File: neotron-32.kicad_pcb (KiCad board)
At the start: 2 copper layers, 166.9 x 140.7 mm, 95 parts, among them J1 Conn_02x06, J10 micro SD Card, J11 Conn_02x13_Top_Bottom, J12 AVR-ISP-6, J13 DE9 Male, J14 DE9 Male, J15 Double-mini-DIN-6, J17 DB15HD_Female, J18 Conn_02x05, J2 Conn_02x06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

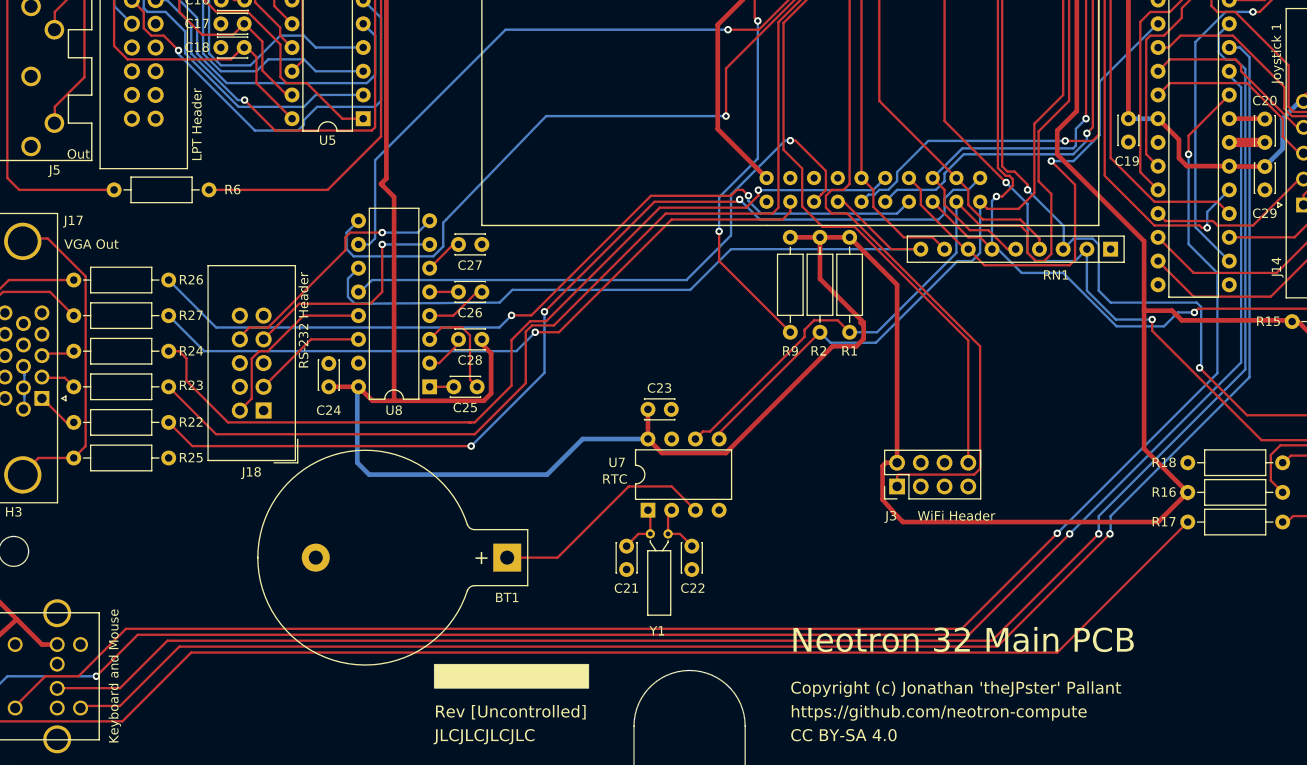
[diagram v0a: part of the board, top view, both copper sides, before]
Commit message: Moved some tracks away from the Neotron silkscreen text.
Also removed some weird trace overlaps near the Wifi connector.
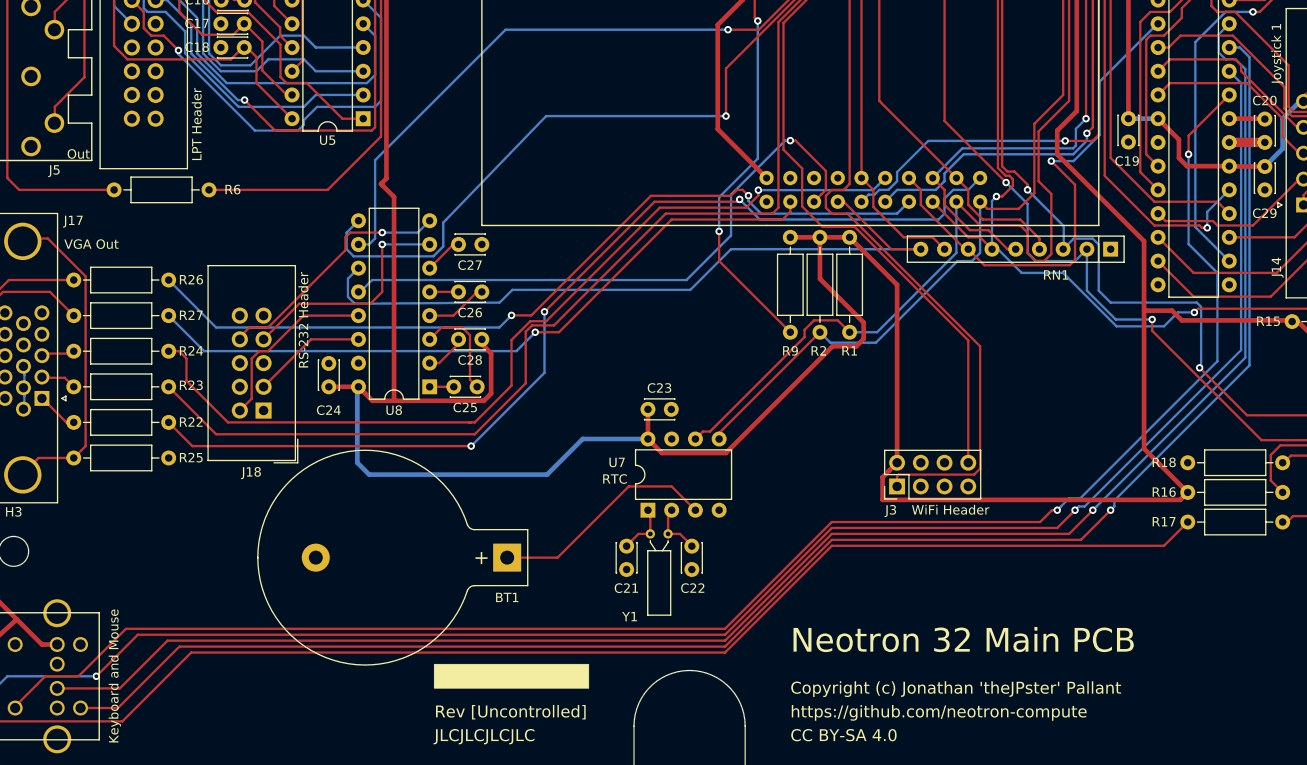
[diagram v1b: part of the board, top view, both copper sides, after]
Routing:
- net +3V3: track 498.1 -> 494.0 mm
- net /Keyboard, Mouse and Joystick/MS_DAT: track 181.7 -> 179.9 mm
- net /Keyboard, Mouse and Joystick/MS_CLK: track 177.7 -> 176.3 mm
- net /Keyboard, Mouse and Joystick/KB_DAT: track 179.9 -> 179.1 mm
- net /Keyboard, Mouse and Joystick/KB_CLK: track 176.4 -> 175.7 mm

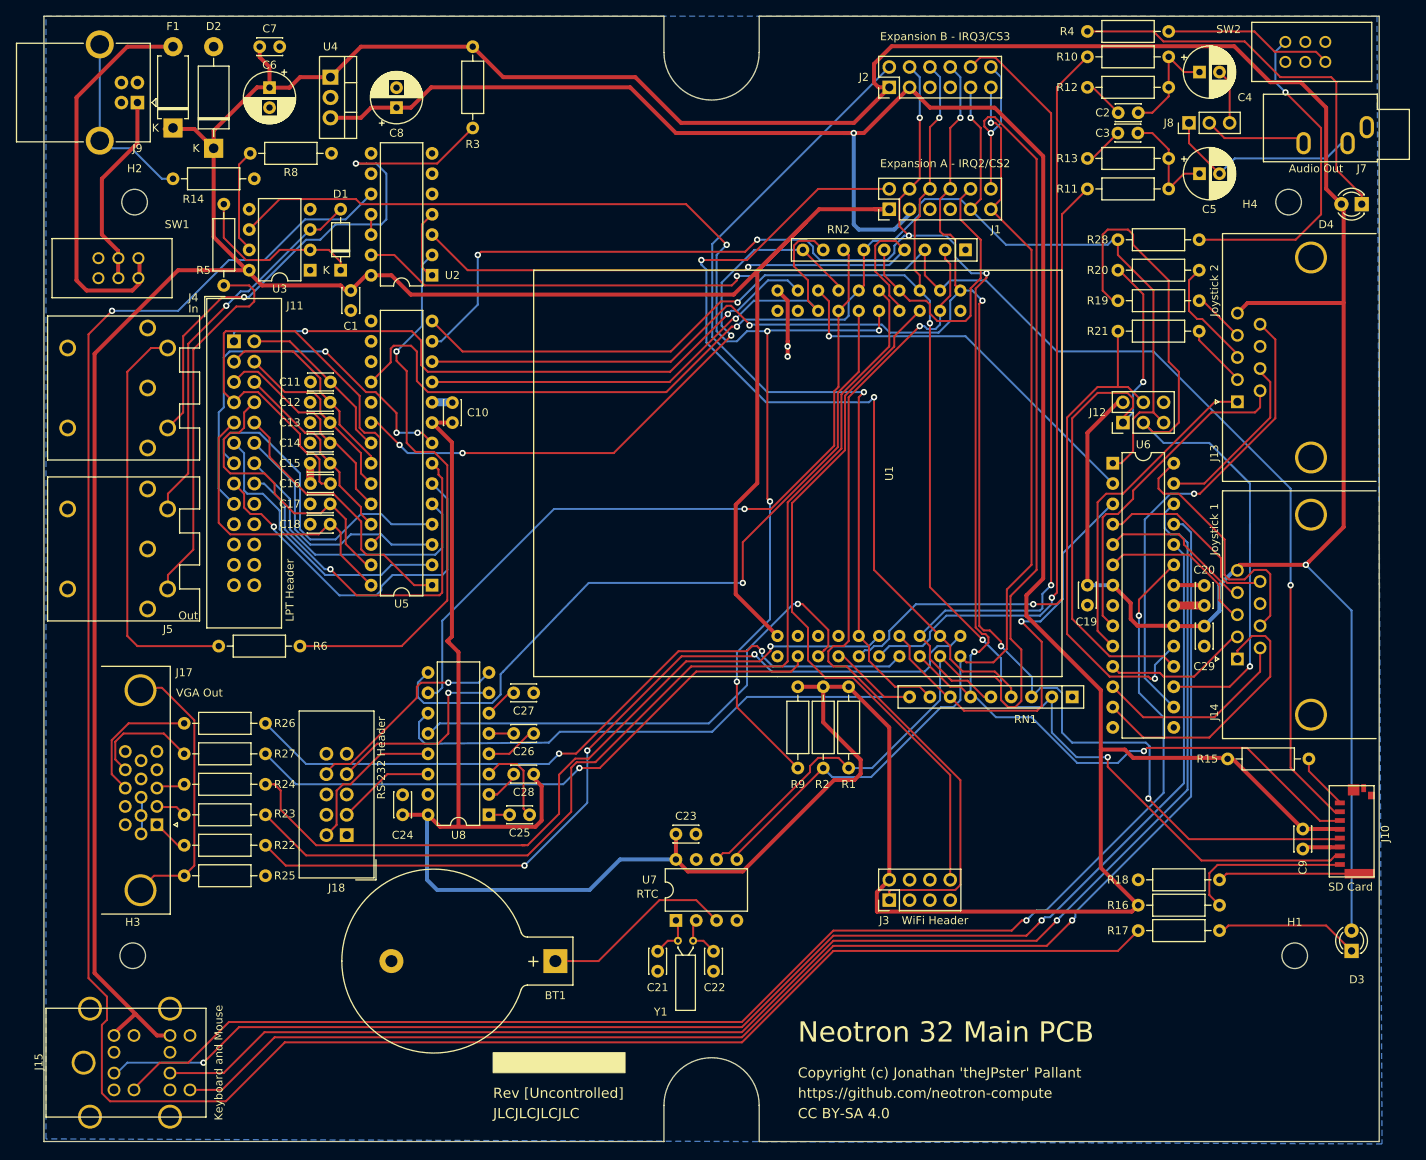
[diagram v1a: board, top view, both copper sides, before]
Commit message: Laying out board again, but on a 50 mil grid for parts.
Will use 25 mil grid for traces. This will hopefully avoid the issue
of traces 'sticking' to legs rather than cleanly going precisely down
the middle. It also looks a lot nicer now everything is properly
aligned.

I've also taken the opportunity to put the expansion slots all next to each other.
Might need to add some support holes for some legs, a la M.2 SSDs.
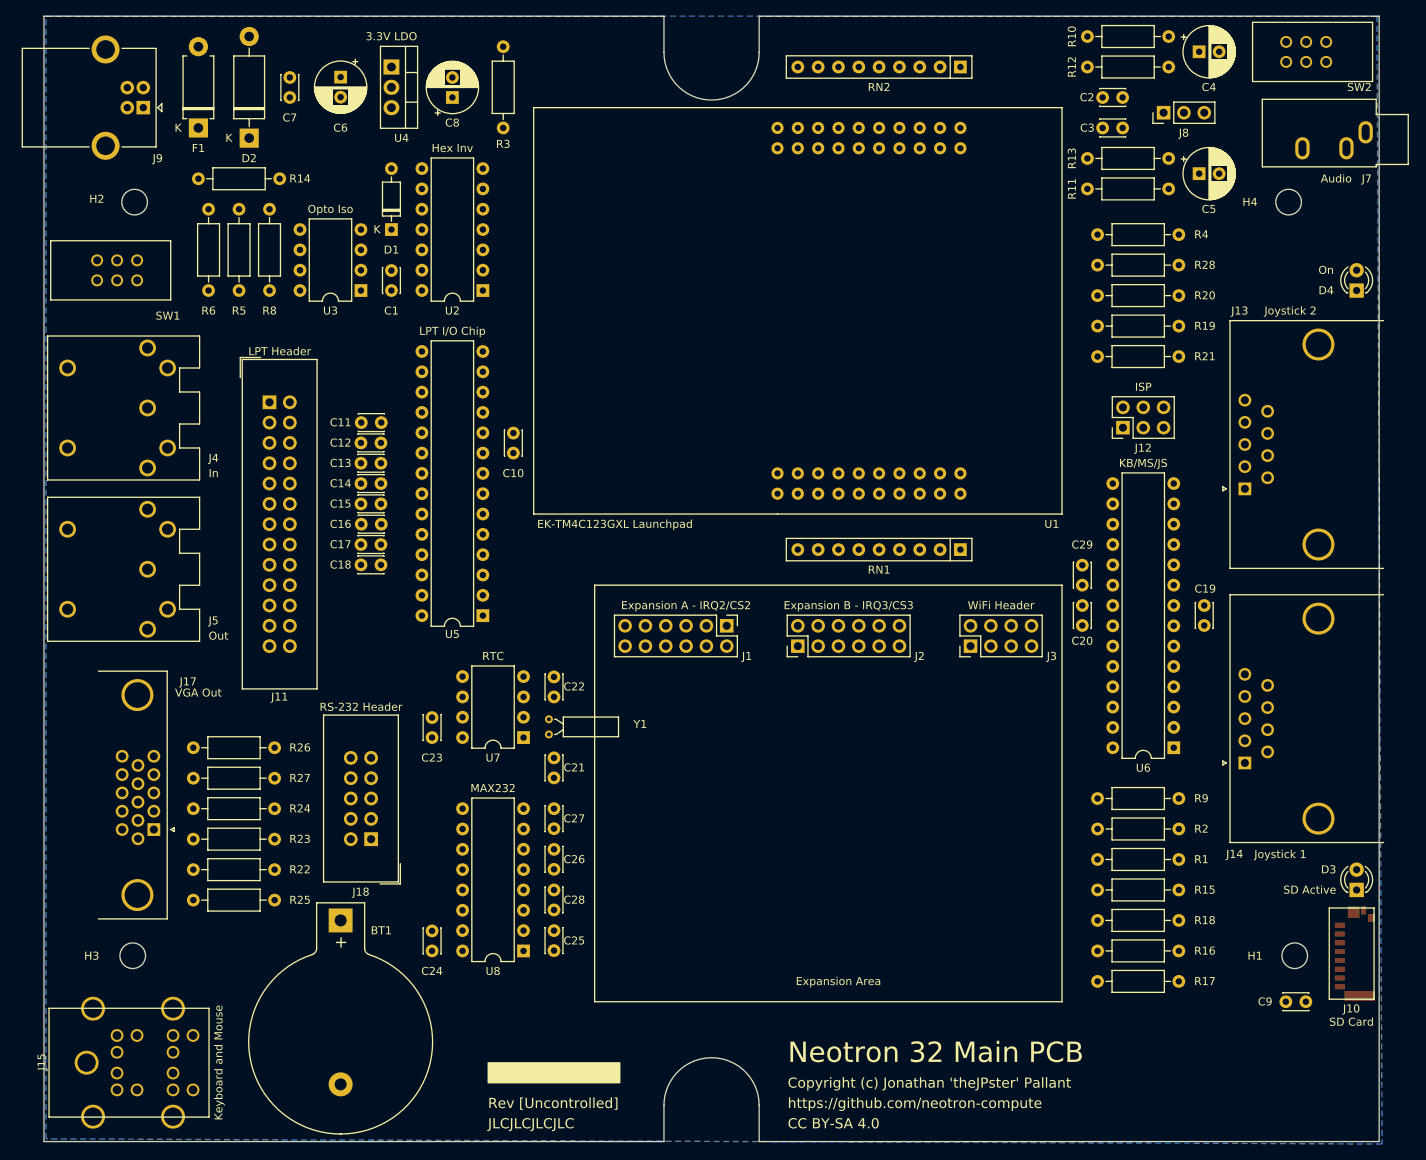
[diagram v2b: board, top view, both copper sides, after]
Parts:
- moved J2 70.8 mm to (165.1, 96.5)
- moved J1 55.9 mm to (156.2, 94.0), turned to 270 degrees
- moved R6 55.8 mm to (91.4, 41.9), turned to 270 degrees
- moved R9 37.7 mm to (202.6, 115.6), turned to 0 degrees
- moved C22 37.5 mm to (134.6, 102.9), turned to 90 degrees
- moved U6 36.4 mm to (212.1, 109.2), turned to 180 degrees
- moved R2 35.1 mm to (202.6, 119.4), turned to 0 degrees
- moved J3 33.3 mm to (186.7, 96.5)
- moved R1 33.1 mm to (202.6, 123.2), turned to 0 degrees
- moved C23 32.8 mm to (119.4, 108.0), turned to 90 degrees
- moved Y1 30.4 mm to (134.0, 107.6), turned to 90 degrees
- moved U7 29.8 mm to (130.8, 108.0), turned to 180 degrees
- moved C21 27.4 mm to (134.6, 113.0)
- moved BT1 27.3 mm to (108.0, 130.8), turned to 270 degrees
- moved R4 25.4 mm to (202.6, 45.1)
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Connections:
- net Net-(F1-Pad2) renamed /Power/UNFUSED_5V
- net Net-(J9-Pad1) renamed /Power/VUSB
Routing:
- net +5V: track 638.8 -> 0.00 mm, vias 1 -> 0
- net +3V3: track 494.0 -> 0.00 mm, vias 1 -> 0
- net Net-(R17-Pad2): track 277.5 -> 0.00 mm, vias 1 -> 0
- net /PA5_SPI_MOSI: track 226.1 -> 0.00 mm, vias 7 -> 0
- net /PA2_SPI_CLK: track 215.4 -> 0.00 mm, vias 5 -> 0
- net /PA4_SPI_MISO: track 208.3 -> 0.00 mm, vias 5 -> 0
- net /Keyboard, Mouse and Joystick/MS_DAT: track 179.9 -> 0.00 mm, vias 1 -> 0
- net /Keyboard, Mouse and Joystick/KB_DAT: track 179.1 -> 0.00 mm, vias 2 -> 0
- net /~PA3_SPI_CS0: track 177.7 -> 0.00 mm, vias 2 -> 0
- net /Keyboard, Mouse and Joystick/MS_CLK: track 176.3 -> 0.00 mm, vias 1 -> 0
- net /Keyboard, Mouse and Joystick/KB_CLK: track 175.7 -> 0.00 mm, vias 2 -> 0
- net /~RESET: track 169.7 -> 0.00 mm, vias 2 -> 0
- net /PC6_MIDI_IN: track 158.4 -> 0.00 mm, vias 5 -> 0
- net /PA6_I2C_SCL: track 154.3 -> 0.00 mm, vias 1 -> 0
- net /PB7_VGA_GREEN: track 132.8 -> 0.00 mm
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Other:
- net class Default: clearance 0.2 -> 0.254; trace_width 0.25 -> 0.254; via_dia 0.8 -> 1.016; via_drill 0.4 -> 0.635
- net class Power: clearance 0.2 -> 0.381; trace_width 0.5 -> 0.508; via_dia 0.8 -> 1.016; via_drill 0.4 -> 0.635
- rule pad_to_mask_clearance: 0.051 -> 0.0508
- rule solder_mask_min_width: 0.25 -> 0.254
- rule trace_clearance: 0.2 -> 0.254
- rule trace_min: 0.2 -> 0.2032
- rule via_min_drill: 0.3 -> 0.3048
- rule via_min_size: 0.4 -> 0.4064
- board text added: "3.3V LDO"
- board text added: "Audio"
- board text added: "EK-TM4C123GXL Launchpad"
- board text added: "Expansion Area"
- board text added: "Hex Inv"
- board text added: "ISP"
- board text added: "KB/MS/JS"
- board text added: "LPT I/O Chip"
- board text added: "MAX232"
- board text added: "On"
- board text added: "Opto Iso"
- board text added: "SD Active"
- board text removed: "Audio Out"

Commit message: Work in progress.
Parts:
- added H5: MountingHole, MountingHole:MountingHole_3.2mm_M3, F.Cu at (149.9, 134.6)
- added H6: MountingHole, MountingHole:MountingHole_3.2mm_M3, F.Cu at (171.4, 134.6)
- moved R9 80.3 mm to (175.3, 40.0), turned to 180 degrees
- moved R3 41.7 mm to (95.2, 57.1), turned to 0 degrees
- moved J2 13.0 mm to (177.8, 94.0), turned to 270 degrees
- moved D4 2.54 mm to (234.9, 49.5), turned to 270 degrees
- moved J7 0.85 mm to (235.2, 32.3)
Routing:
- net +5V: track 0.00 -> 493.0 mm
- net +3V3: track 0.00 -> 191.4 mm
- net /~RESET: track 0.00 -> 177.6 mm
- net /PA7_I2C_SDA: track 0.00 -> 112.0 mm, vias 0 -> 1
- net /PA6_I2C_SCL: track 0.00 -> 111.8 mm
- net /~PA3_SPI_CS0: track 0.00 -> 101.0 mm, vias 0 -> 1
- net Net-(R28-Pad2): track 0.00 -> 83.5 mm
- net /PA4_SPI_MISO: track 0.00 -> 73.2 mm, vias 0 -> 2
- net /PA2_SPI_CLK: track 0.00 -> 70.8 mm, vias 0 -> 2
- net /PE5_AUDIO_R: track 0.00 -> 69.0 mm
- net /Keyboard, Mouse and Joystick/SELECT_JS2: track 0.00 -> 68.8 mm
- net /PA5_SPI_MOSI: track 0.00 -> 67.8 mm, vias 0 -> 1
- net Net-(J9-Pad5): track 0.00 -> 57.1 mm
- net /PE4_AUDIO_L: track 0.00 -> 55.7 mm
- net /~PE3_IRQ2: track 0.00 -> 53.2 mm
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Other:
- net class Power: clearance 0.381 -> 0.254
- rule pad_to_mask_clearance: 0.0508 -> 0.0254

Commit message: Work tracing done.
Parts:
- moved R17 7.62 mm to (212.7, 130.8)
- moved R18 7.62 mm to (212.7, 138.4)
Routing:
- net /Keyboard, Mouse and Joystick/KB_CLK: track 0.00 -> 178.3 mm, vias 0 -> 1
- net /Keyboard, Mouse and Joystick/KB_DAT: track 0.00 -> 168.8 mm, vias 0 -> 1
- net /Keyboard, Mouse and Joystick/MS_DAT: track 0.00 -> 166.4 mm, vias 0 -> 1
- net /Keyboard, Mouse and Joystick/MS_CLK: track 0.00 -> 162.0 mm, vias 0 -> 1
- net Net-(R17-Pad2): track 0.00 -> 140.6 mm, vias 0 -> 1
- net /~PA3_SPI_CS0: track 101.0 -> 231.7 mm, vias 1 -> 3
- net +3V3: track 191.4 -> 320.6 mm, vias 0 -> 3
- net /PE0_U7RX: track 0.00 -> 115.5 mm, vias 0 -> 1
- net /PC6_MIDI_IN: track 5.72 -> 85.9 mm, vias 0 -> 2
- net /PA2_SPI_CLK: track 70.8 -> 144.3 mm, vias 2 -> 3
- net /PD6_U2RX: track 0.00 -> 68.5 mm, vias 0 -> 2
- net Net-(D1-Pad2): track 0.00 -> 65.1 mm, vias 0 -> 1
- net /PA5_SPI_MOSI: track 67.8 -> 131.8 mm, vias 1 -> 2
- net /PE1_U7TX: track 15.3 -> 74.9 mm, vias 0 -> 1
- net /PA4_SPI_MISO: track 73.2 -> 132.2 mm, vias 2 -> 1
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
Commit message: More tracking.
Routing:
- net /PB4_VGA_HSYNC: track 0.00 -> 190.3 mm, vias 0 -> 1
- net /PB7_VGA_GREEN: track 0.00 -> 124.2 mm
- net /PC5_U1CTS: track 0.00 -> 123.5 mm, vias 0 -> 1
- net /PF1_VGA_RED: track 0.00 -> 115.0 mm
- net /~PB2_STROBE: track 0.00 -> 114.0 mm
- net /PB1_U1TX: track 9.09 -> 120.9 mm, vias 0 -> 2
- net /PD3_VGA_BLUE: track 0.00 -> 94.0 mm, vias 0 -> 1
- net /PB0_U1RX: track 0.00 -> 84.5 mm, vias 0 -> 2
- net /~PF0_IRQ1: track 9.72 -> 92.2 mm
- net /PB5_VGA_VSYNC: track 0.00 -> 81.9 mm, vias 0 -> 1
- net /~PB6_SPI_CS2: track 28.5 -> 103.7 mm, vias 0 -> 1
- net /Parallel Printer/RESET: track 0.00 -> 73.8 mm, vias 0 -> 1
- net /Parallel Printer/~LF: track 0.00 -> 69.3 mm
- net /PD7_U2TX: track 11.2 -> 80.4 mm, vias 0 -> 1
- net /PC7_MIDI_OUT: track 11.2 -> 80.4 mm, vias 0 -> 1
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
